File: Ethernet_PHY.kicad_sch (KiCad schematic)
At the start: 16 parts, among them J2 RJ45_Hanrun_HR911105A_Horizon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, U7 LAN8720A, Y1 25MHz

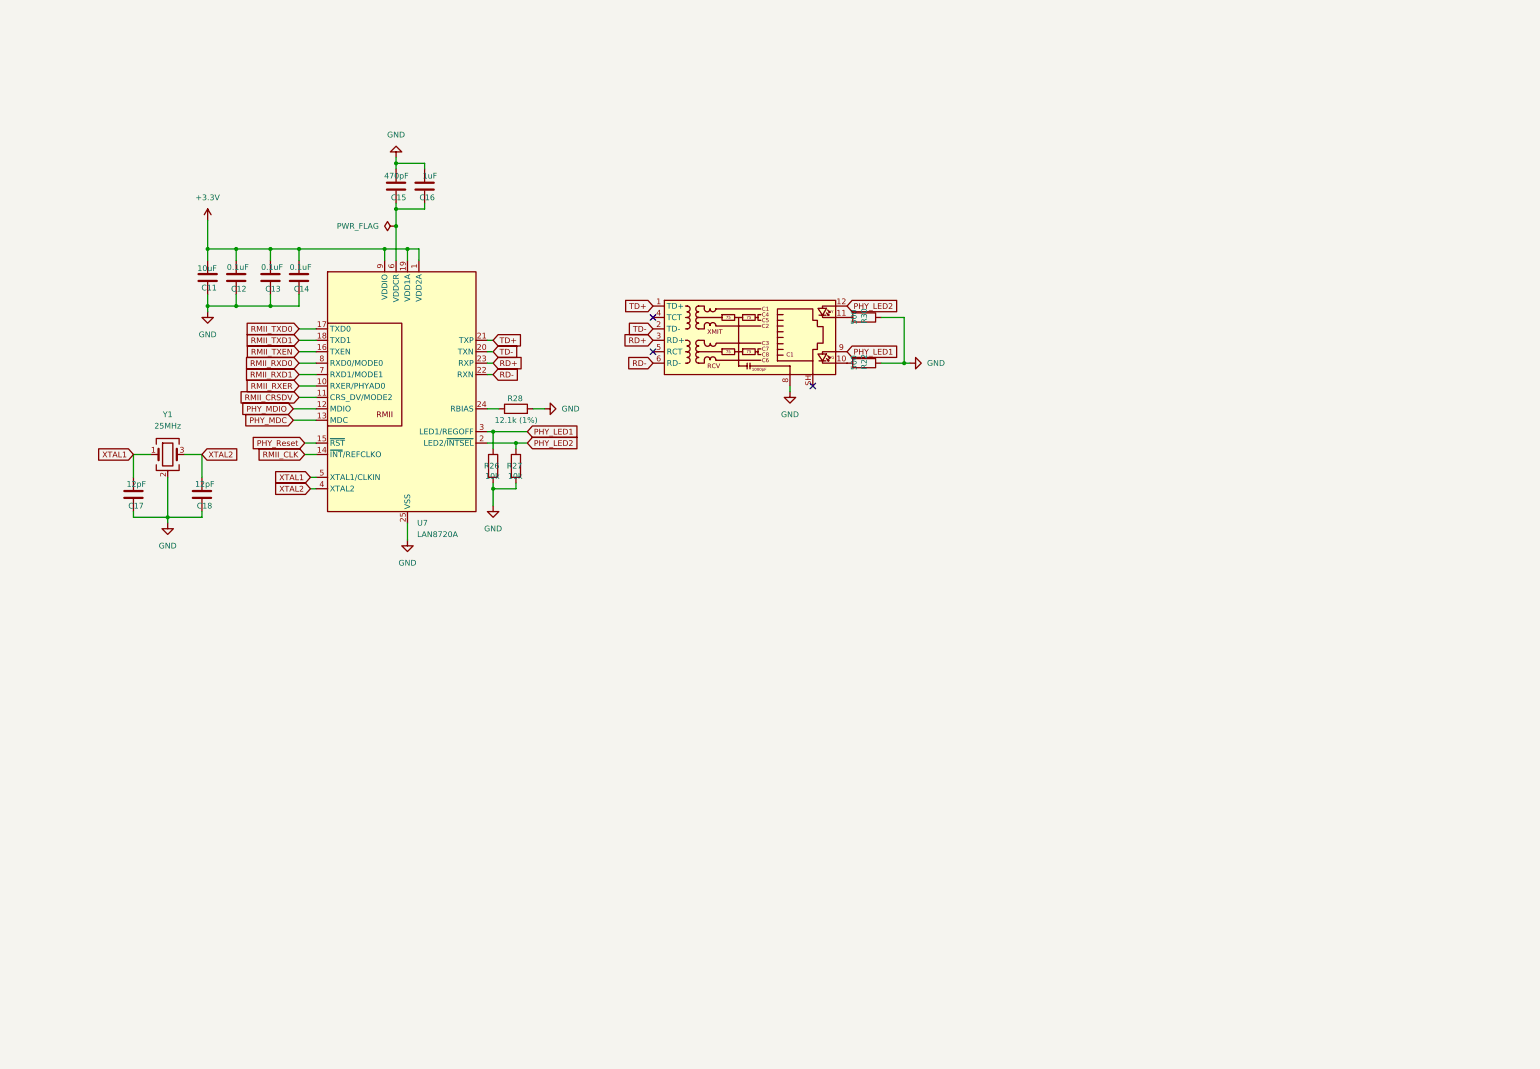
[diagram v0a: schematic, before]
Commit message: ESP32 P4 with 8 Ethernet
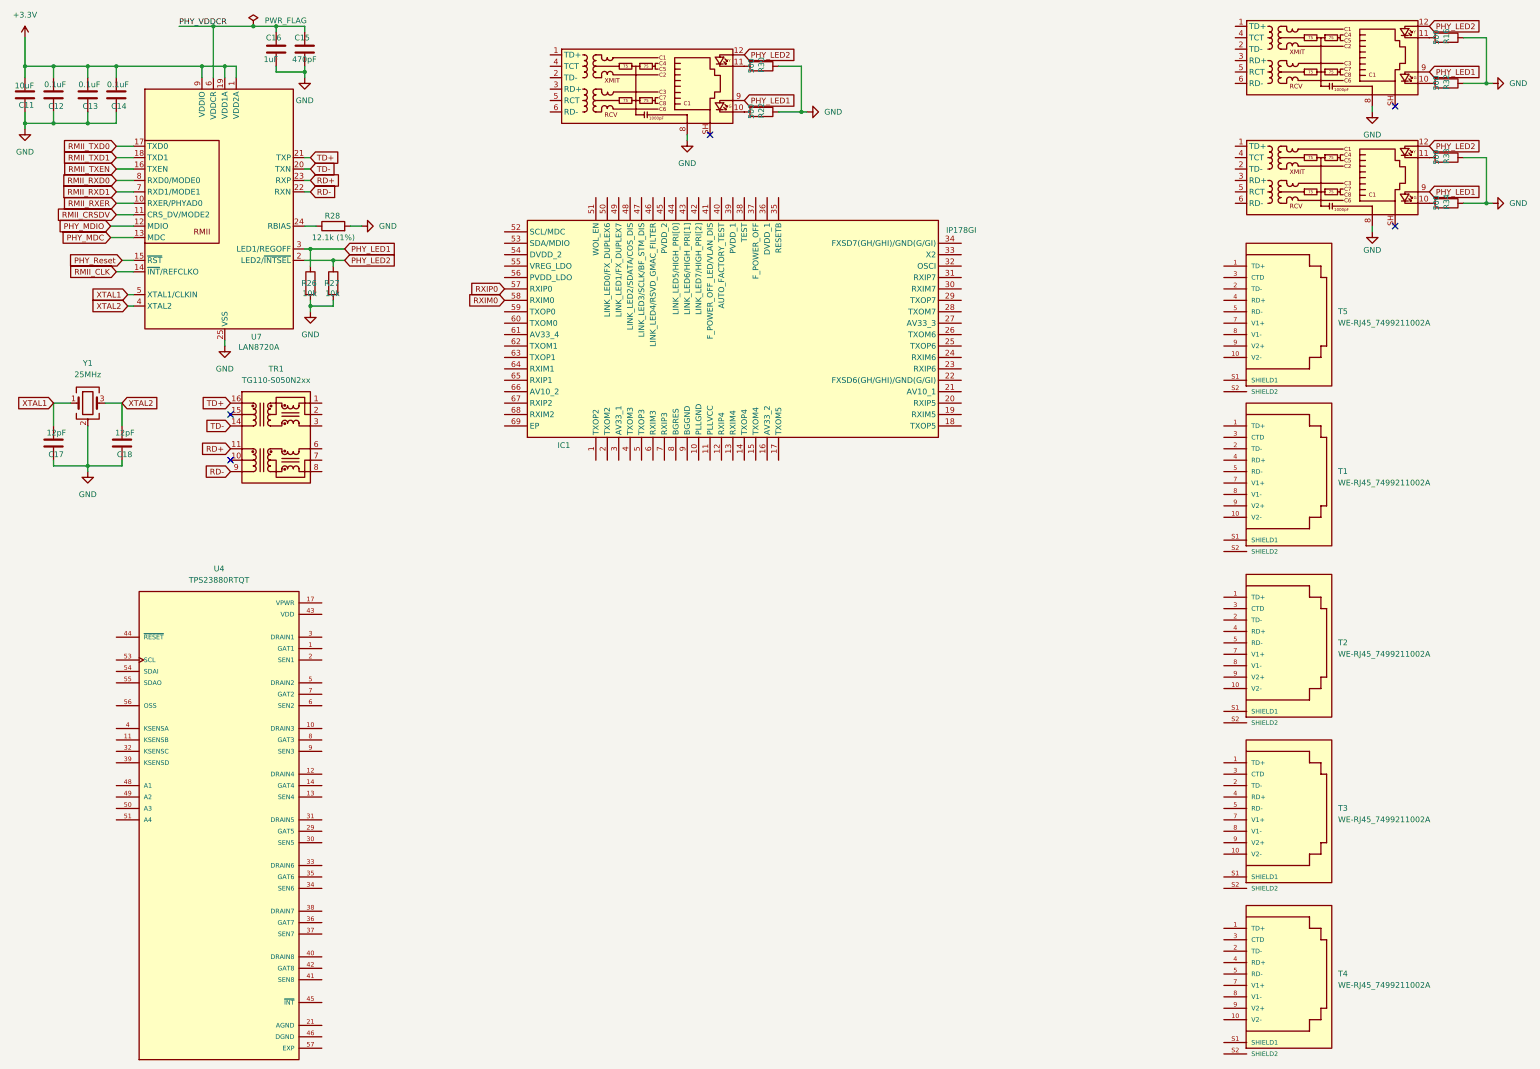
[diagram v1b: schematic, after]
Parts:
- added IC1: IP178GI, Custom_Footprint:IP178GI, symbol IP178GI:IP178GI
- added J13, J14: RJ45_Hanrun_HR911105A_Horizontal, Connector_RJ:RJ45_Hanrun_HR911105A_Horizontal, symbol Connector:RJ45_Hanrun_HR911105A_Horizontal
- added R16, R32, R33, R34: 500, Resistor_SMD:R_0603_1608Metric, symbol Device:R
- added T1, T2, T3, T4, T5: WE-RJ45_7499211002A, Custom_Footprint:WE-RJ45_7499211002A, symbol WE-RJ45_7499211002A:WE-RJ45_7499211002A
- added TR1: TG110-S050N2xx, Transformer_SMD:Transformer_Ethernet_Halo_N2_SO-16_7.11x12.7mm, symbol Transformer:TG110-S050N2xx
- added U4: TPS23880RTQT, Custom_Footprint:TPS23880RTQT, symbol TPS23880RTQT:TPS23880RTQT
- R22, R26, R27, R28, R30: footprint (none) -> Resistor_SMD:R_0603_1608Metric
- Y1: footprint (none) -> Oscillator:Oscillator_SMD_SiT_PQFN-4Pin_5.0x3.2mm
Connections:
- net GND: now also J13.8, J14.8, R16.1, R32.1, R33.1, R34.1
- net PHY_LED1: now also J13.9, J14.9
- net PHY_LED2: now also J13.12, J14.12
- net RD+: now also TR1.11 (RD-); no longer J2.3 (RD+)
- net RD-: now also TR1.9 (RD+); no longer J2.6 (RD-)
- net TD+: now also TR1.16 (TD-); no longer J2.1 (TD+)
- net TD-: now also TR1.14 (TD+); no longer J2.2 (TD-)
- net PHY_VDDCR: now reaches C15.1, C16.1, U7.6 (VDDCR)
- new net: J14.10, R34.2
- new net: J13.10, R32.2
- new net: J13.11, R16.2
- new net: J14.11, R33.2
- new net RXIM0: IC1.58 (RXIM0)
- new net RXIP0: IC1.57 (RXIP0)
- no-connect marks 3 -> 5
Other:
- moved on the sheet: C11, C12, C13, C14, C15, C16, C17, C18, R22, R26, R27, R28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
